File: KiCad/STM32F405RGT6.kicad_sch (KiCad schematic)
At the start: 40 parts, among them J1 USB_C_Receptacle_USB2.0, SW1 SW_SPST, U1 STM32F405RGTx, U2 M24C02-RMN, Y1 25MHz

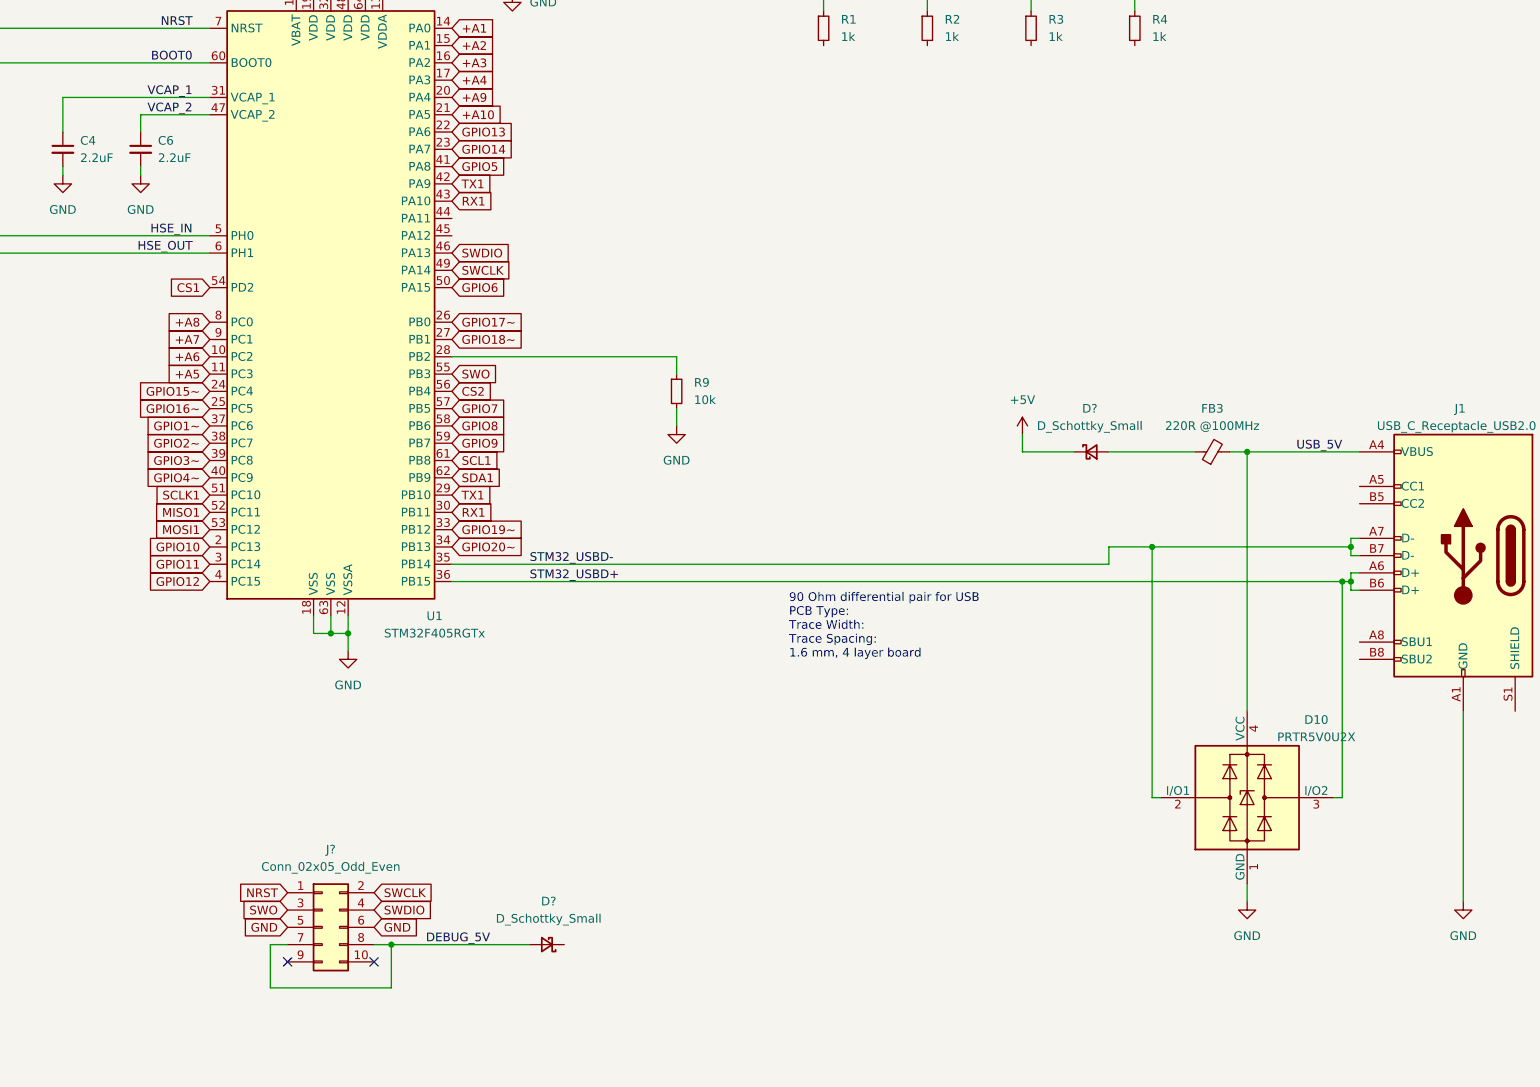
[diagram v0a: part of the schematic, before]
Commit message: Updated Schematic to STM32 software
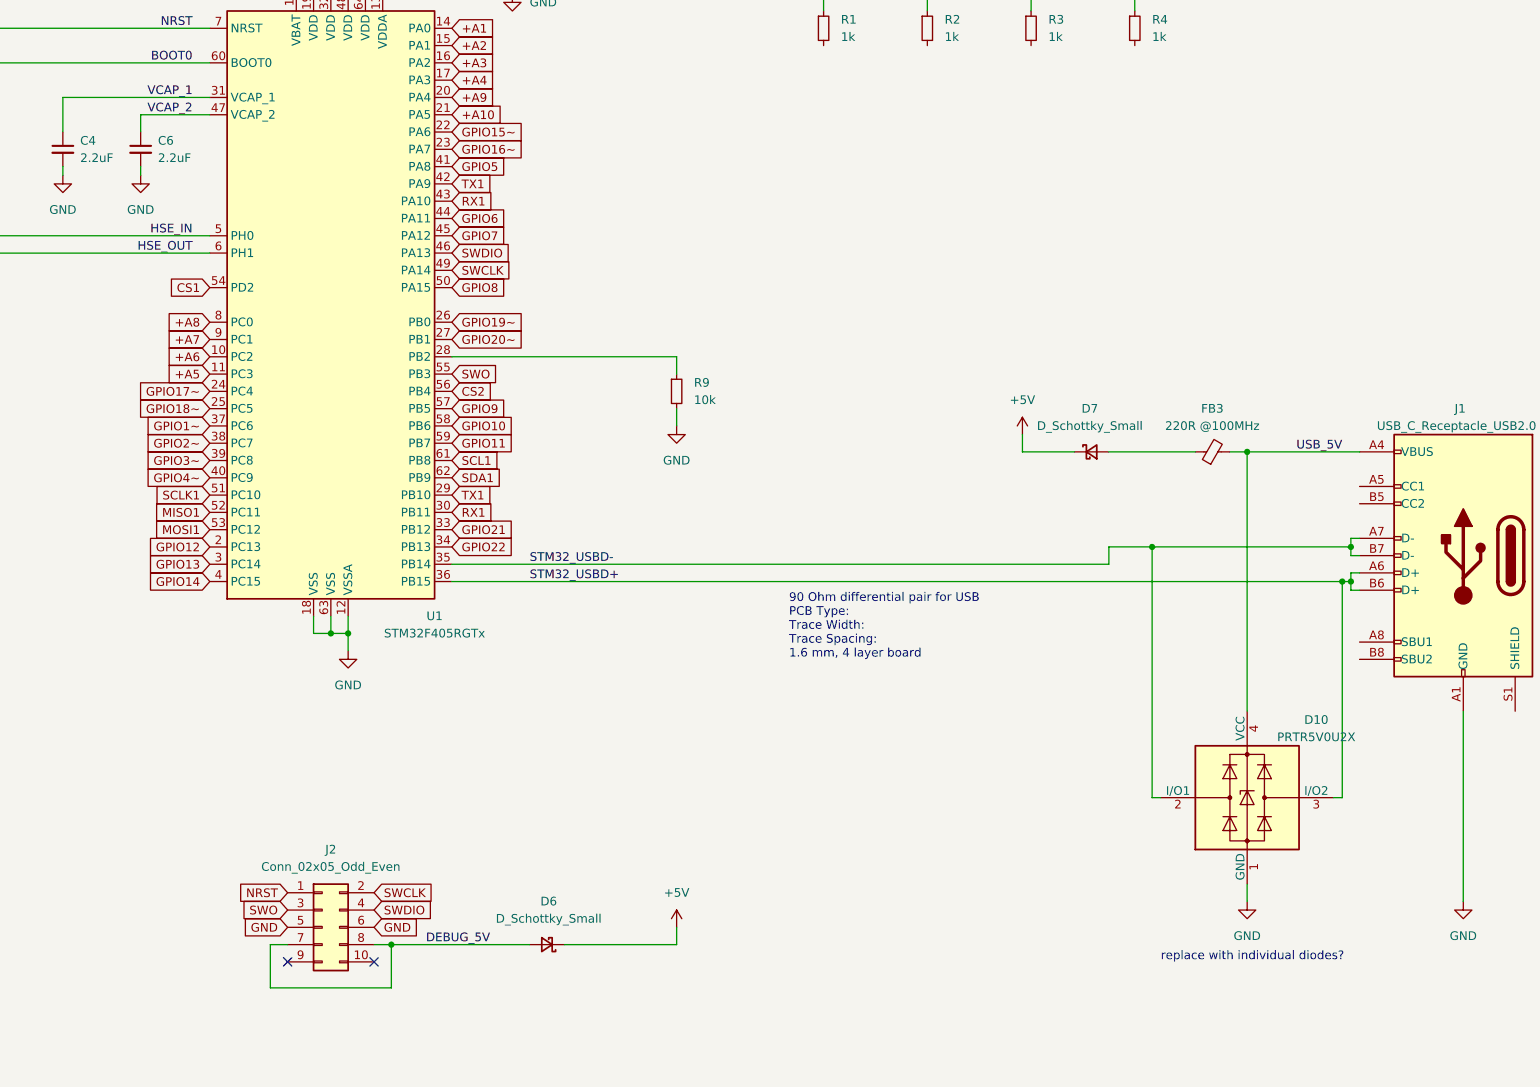
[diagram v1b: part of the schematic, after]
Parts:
- gave numbers to parts that had none: 3
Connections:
- net +5V: now also D6.1 (K)
- net GPIO10: now also U1.58 (PB6); no longer U1.2 (PC13)
- net GPIO11: now also U1.59 (PB7); no longer U1.3 (PC14)
- net GPIO12: now also U1.2 (PC13); no longer U1.4 (PC15)
- net GPIO13: now also U1.3 (PC14); no longer U1.22 (PA6)
- net GPIO14: now also U1.4 (PC15); no longer U1.23 (PA7)
- net GPIO15~: now also U1.22 (PA6); no longer U1.24 (PC4)
- net GPIO16~: now also U1.23 (PA7); no longer U1.25 (PC5)
- net GPIO17~: now also U1.24 (PC4); no longer U1.26 (PB0)
- net GPIO18~: now also U1.25 (PC5); no longer U1.27 (PB1)
- net GPIO19~: now also U1.26 (PB0); no longer U1.33 (PB12)
- net GPIO20~: now also U1.27 (PB1); no longer U1.34 (PB13)
- net GPIO6: now also U1.44 (PA11); no longer U1.50 (PA15)
- net GPIO7: now also U1.45 (PA12); no longer U1.57 (PB5)
- net GPIO8: now also U1.50 (PA15); no longer U1.58 (PB6)
- net GPIO9: now also U1.57 (PB5); no longer U1.59 (PB7)
- new net GPIO21: U1.33 (PB12)
- new net GPIO22: U1.34 (PB13)
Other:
- note added: "replace with individual diodes?"

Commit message: Updated Schematic and BOM
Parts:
- removed D10: PRTR5V0U2X, Package_TO_SOT_SMD:SOT-143, symbol Power_Protection:PRTR5V0U2X
- added C14, C15: 10uF, Capacitor_SMD:C_0603_1608Metric, symbol Device:C_Small
- added D9: 1N5819WS, Diode_SMD:D_SOD-323, symbol Device:D_Schottky_Small
- added U3: AMS1117-3.3, Package_TO_SOT_SMD:SOT-223-3_TabPin2, symbol Regulator_Linear:AMS1117-3.3
- added U4: SRV05-4, Package_TO_SOT_SMD:SOT-23-6, symbol Power_Protection:SRV05-4
- D6, D7: value D_Schottky_Small -> 1N5819WS; footprint (none) -> Diode_SMD:D_SOD-323; JLCPCB Part # (none) -> C191023; Part Number (none) -> 1N5819WS
- J2: footprint (none) -> Connector_PinHeader_2.54mm:PinHeader_2x05_P2.54mm_Vertical; JLCPCB Part # (none) -> C124387; Part Number (none) -> B-2100S10P-B110
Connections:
- net +3V3: now also D9.1 (K)
- net +5V: now also C14.1, U3.3 (VI)
- net GND: now also C14.2, C15.2, U3.1 (GND), U4.2 (VN)
- net STM32_USBD+: now also U4.3 (IO2)
- net STM32_USBD-: now also U4.1 (IO1)
- net USB_5V: now also U4.5 (VP)
- new net ONBOARD_+3V3: C15.1, D9.2 (A), U3.2 (VO)
- no-connect marks 3 -> 5
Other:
- note removed: "replace with individual diodes?"
- moved on the sheet: D6, J2

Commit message: Updated PCB and Schematic
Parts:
- added C16: 100nF, Capacitor_SMD:C_0603_1608Metric, symbol Device:C_Small
- added SW2: TS-1187A, Button_Switch_SMD:SW_SPST_SKQG_WithStem, symbol Switch:SW_SPST
- J1: footprint https://datasheet.lcsc.com/lcsc/2205251630_Korean-Hroparts-Elec-TYPE-C-31-M-12_C165948.pdf -> Connector_USB:USB_C_Receptacle_HRO_TYPE-C-31-M-12
- SW1: value SW_SPST -> TS-1187A; footprint (none) -> Button_Switch_SMD:SW_SPST_SKQG_WithStem; JLCPCB Part # (none) -> C318884; Part Number (none) -> TS-1187A-B-A-B
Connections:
- net LED_DIN is gone; now on net +3V3: D4.4 (DIN)
- net +3V3: now also D1.2 (A), D2.2 (A), D3.2 (A), D5.2 (A), R1.2, R2.2, R3.2, R4.2, C16.1, SW2.2 (B)
- net GND: now also C16.2, SW2.1 (A)
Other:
- moved on the sheet: C14, C15, C17, D1, D2, D3, D4, D5, D8, D9, R1, R2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

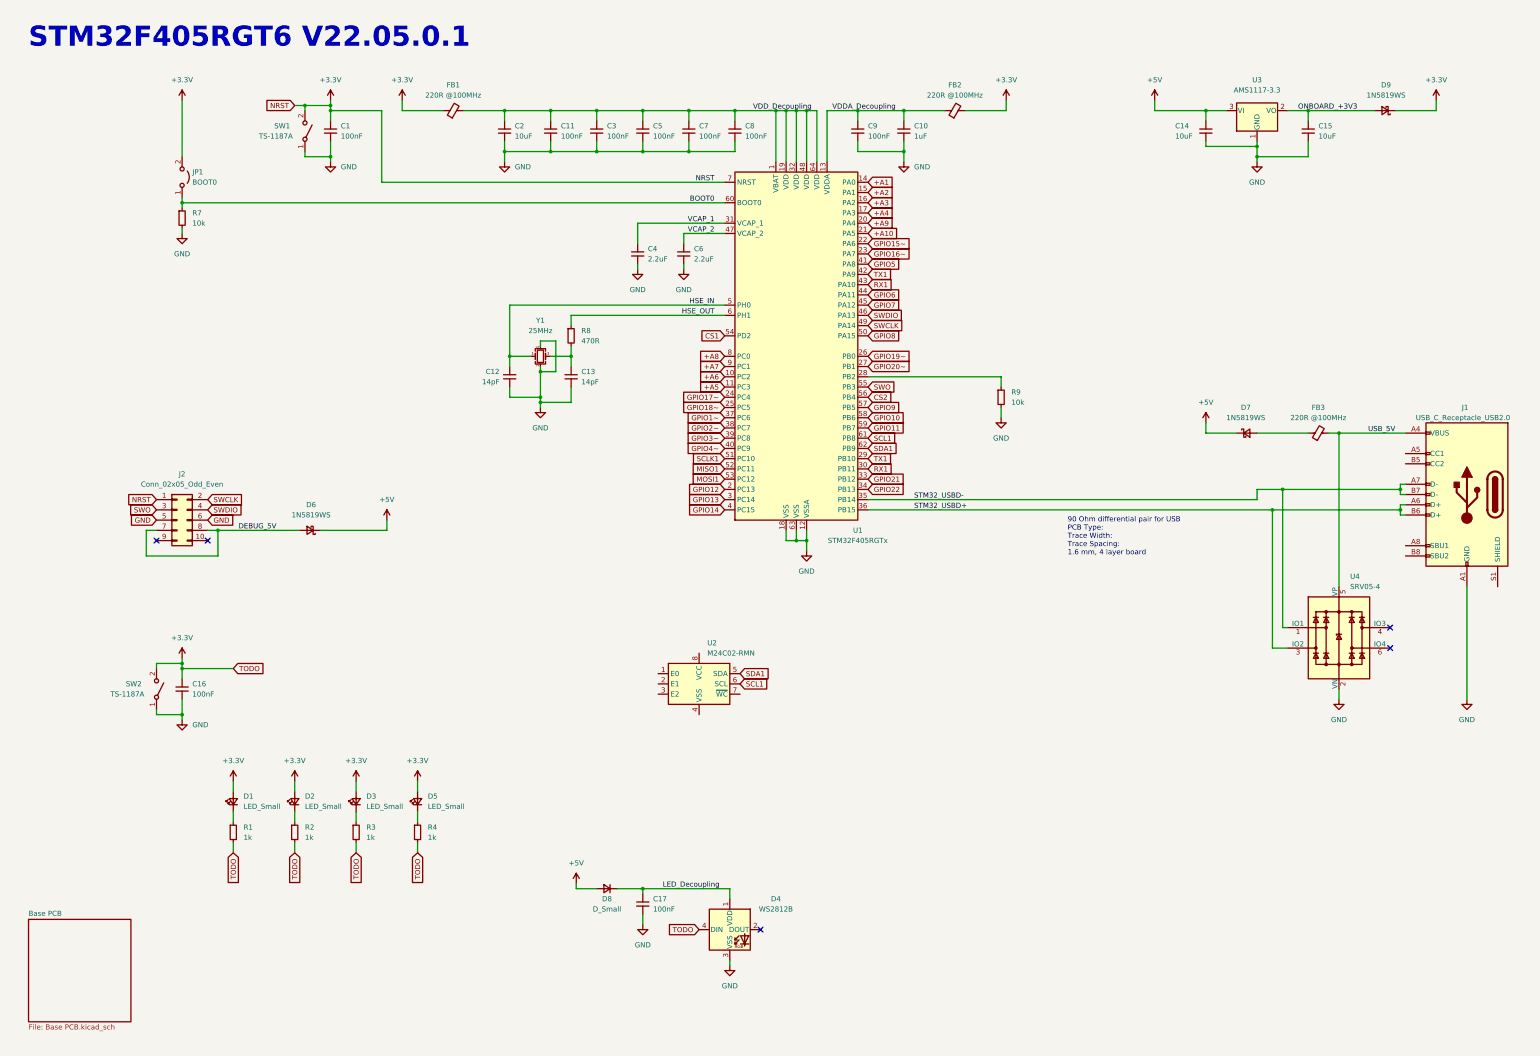
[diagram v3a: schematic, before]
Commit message: Added CCU Resistors
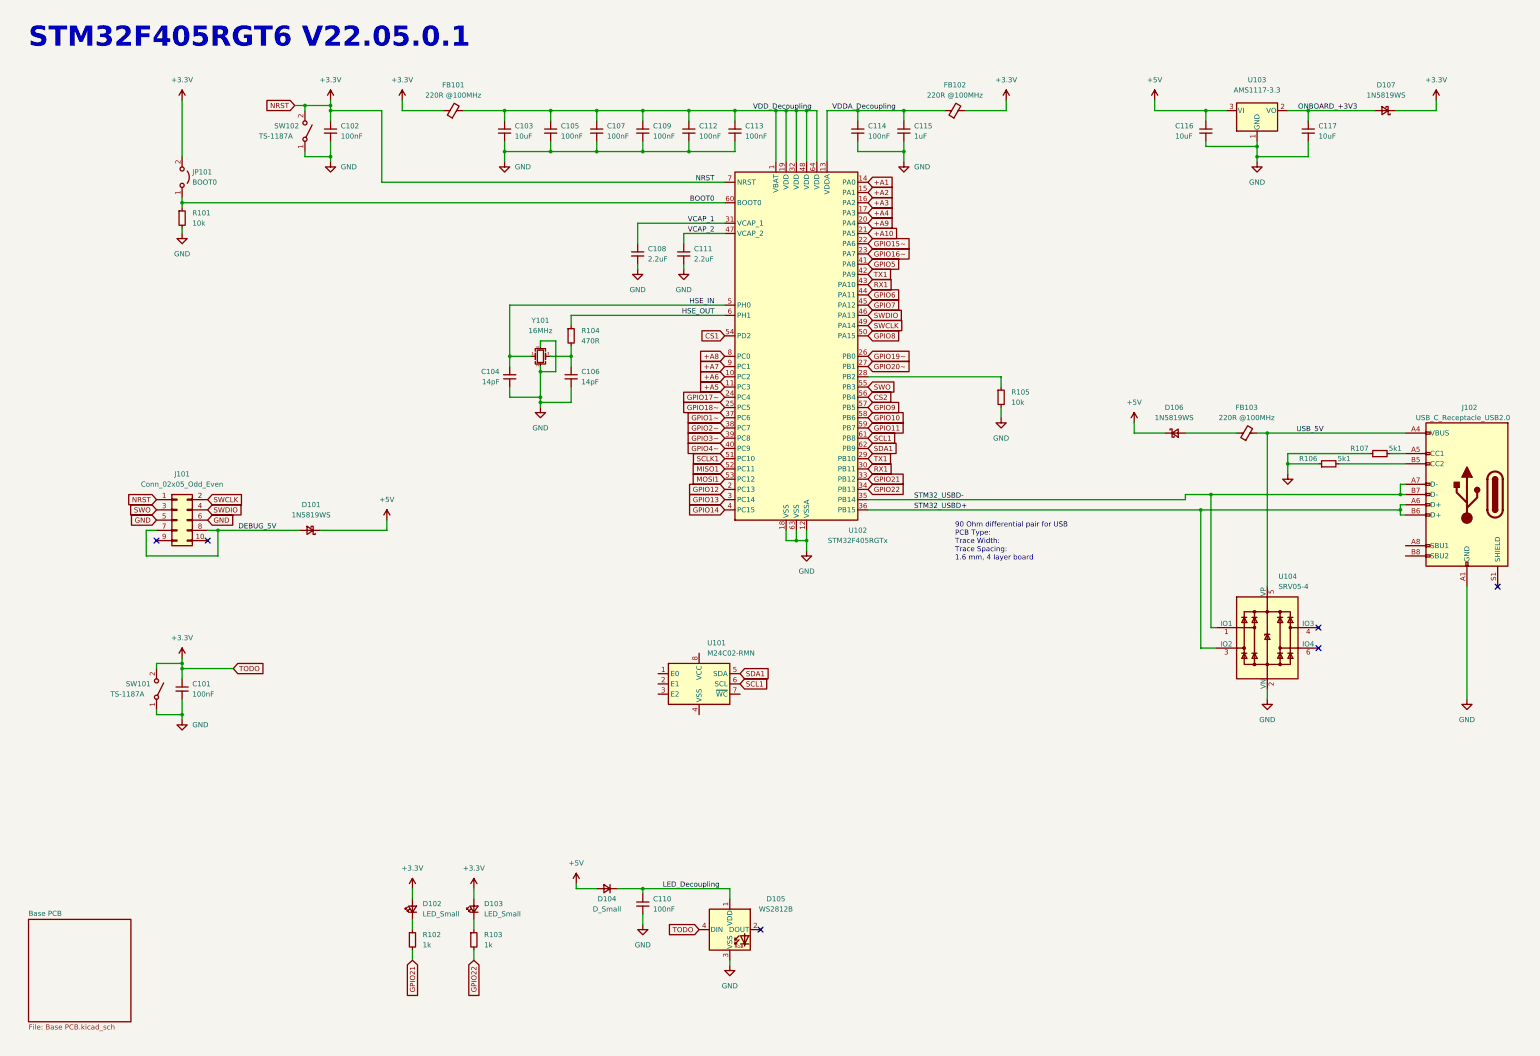
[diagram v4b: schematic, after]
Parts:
- removed D3, D5: LED_Small, LED_SMD:LED_0603_1608Metric, symbol Device:LED_Small
- removed R3, R4: 1k, Resistor_SMD:R_0603_1608Metric, symbol Device:R_Small
- added R106, R107: 5k1, symbol Device:R_Small
- Y101: renamed from Y1; value 25MHz -> 16MHz
- renumbered C16 to C101, C1 to C102, C2 to C103, C12 to C104, C11 to C105, C13 to C106, C3 to C107, C4 to C108, C5 to C109, C17 to C110, C6 to C111, C7 to C112, C8 to C113, C9 to C114, C10 to C115, C14 to C116, C15 to C117, D6 to D101, D1 to D102, D2 to D103, D8 to D104, D4 to D105, D7 to D106, D9 to D107, FB1 to FB101, FB2 to FB102, FB3 to FB103, J2 to J101, J1 to J102, JP1 to JP101, R7 to R101, R1 to R102, R2 to R103, R8 to R104, R9 to R105, SW2 to SW101, SW1 to SW102, U2 to U101, U1 to U102, U3 to U103, U4 to U104
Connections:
- net +3V3: no longer R102.2, R103.2
- net GND: now also R106.1, R107.1
- net GPIO21: now also R102.2
- net GPIO22: now also R103.2
- net at J102.A5 (CC1): now also R107.2
- net at J102.B5 (CC2): now also R106.2
- no-connect marks 5 -> 6
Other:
- moved on the sheet: D102, D103, D106, FB103, R102, R103, U104

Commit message: Updated to newer MEPOS Library
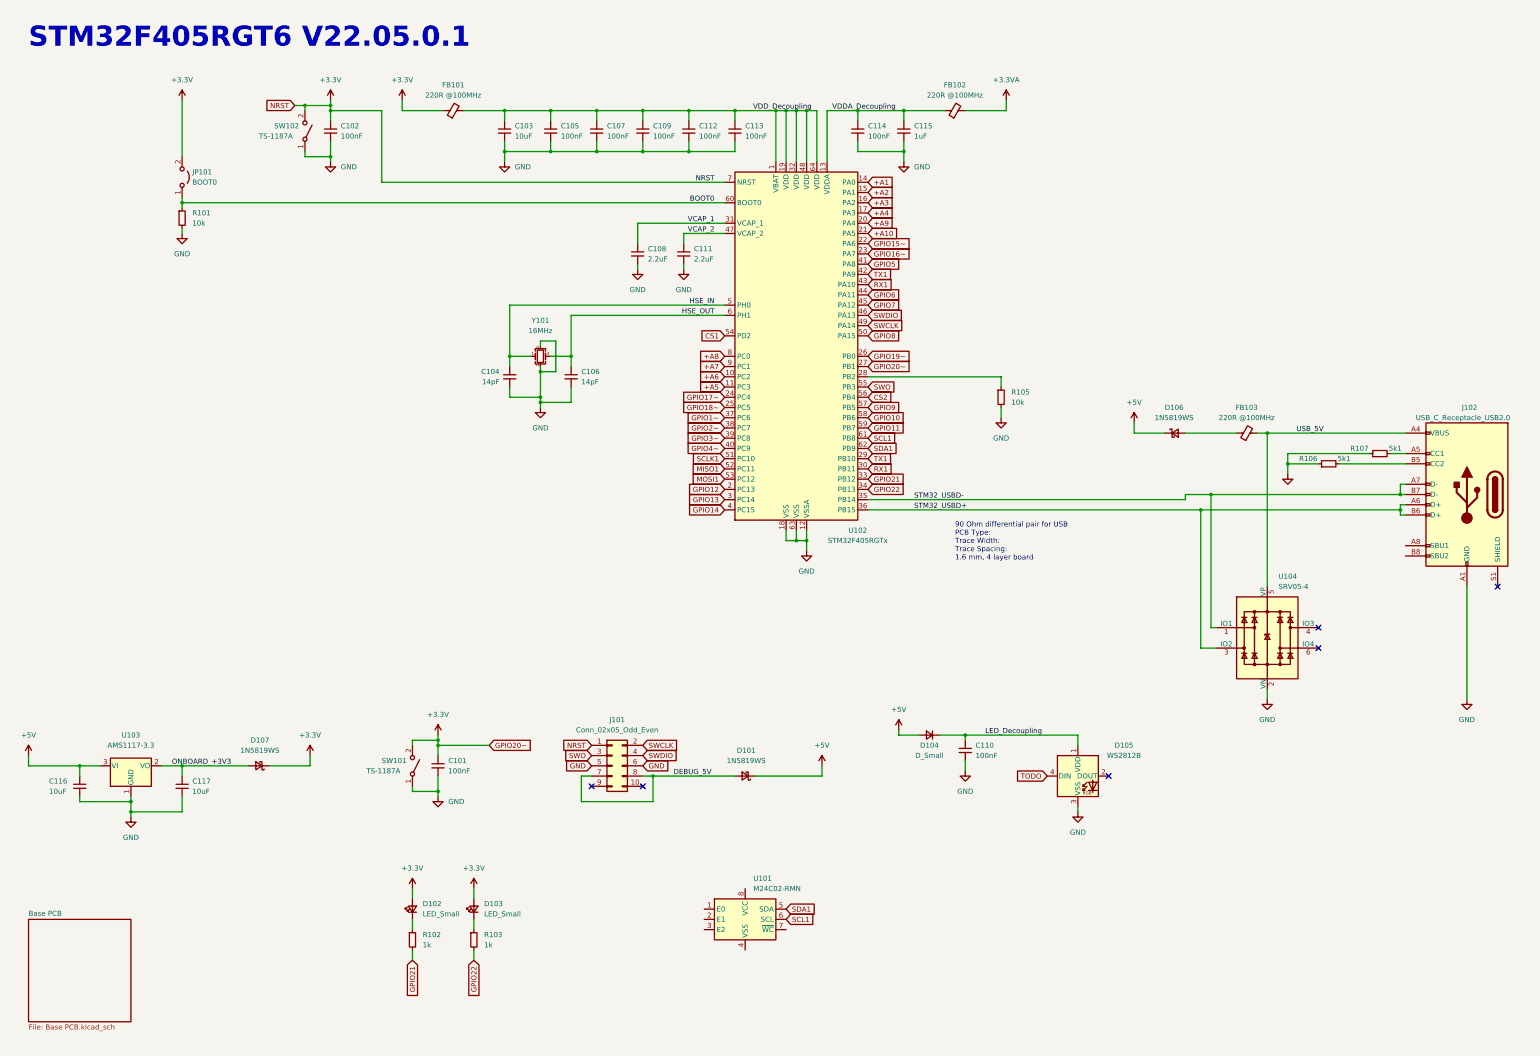
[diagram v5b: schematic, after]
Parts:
- removed R104: 470R, Resistor_SMD:R_0603_1608Metric, symbol Device:R_Small
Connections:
- net GPIO20~ is gone; now on net +3V3: U102.27 (PB1)
- net +3V3: no longer D105.4 (DIN), FB102.2
- net HSE_OUT: now also C106.1, Y101.3
- new net +3.3VA: FB102.2
- new net TODO: D105.4 (DIN)
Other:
- moved on the sheet: C101, C110, C116, C117, D101, D104, D105, D107, J101, SW101, U101, U103

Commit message: Updated Schematic and PCB
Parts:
- added JP2: EXT +3V3A, Connector_PinHeader_2.54mm:PinHeader_1x02_P2.54mm_Vertical, symbol Jumper:Jumper_2_Open
- R5: renamed from R107; footprint (none) -> Resistor_SMD:R_0603_1608Metric
- R6: renamed from R106; footprint (none) -> Resistor_SMD:R_0603_1608Metric
- Y1: renamed from Y101; JLCPCB Part # (none) -> C13738; Part Number (none) -> X322516MLB4SI
- renumbered C116 to C1, C108 to C10, C109 to C11, C111 to C12, C112 to C13, C113 to C14, C114 to C15, C115 to C16, C110 to C17, C117 to C2, C102 to C3, C101 to C4, C103 to C5, C104 to C6, C105 to C7, C106 to C8, C107 to C9, D107 to D1, D102 to D2, D103 to D3, D101 to D4, D104 to D5, D105 to D6, D106 to D7, FB101 to FB1, FB102 to FB2, FB103 to FB3, J101 to J1, J102 to J2, JP101 to JP1, R101 to R1, R102 to R2, R103 to R3, R105 to R4, SW102 to SW1, SW101 to SW2, U103 to U1, U101 to U2, U102 to U3, U104 to U4
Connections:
- net +3.3VA: now also JP2.2 (B)
- net +3V3: now also JP2.1 (A); no longer C4.1, J1.1 (Pin_1), SW2.2 (B), U3.27 (PB1)
- net USB_CC2: now reaches J2.B5 (CC2), R6.2
- net USB_CC1: now reaches J2.A5 (CC1), R5.2
- new net GPIO20~: C4.1, SW2.2 (B), U3.27 (PB1)
- new net NRST: J1.1 (Pin_1)
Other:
- moved on the sheet: R5, R6
